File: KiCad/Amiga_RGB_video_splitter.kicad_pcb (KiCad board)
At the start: 4 copper layers, 57.5 x 60 mm, 26 parts, among them J1 DB23_Female-Connector, J2 DB15_Female_HighDensity_Mount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, J3 KMDGX-9S-BS-1, J4 PJ-320A, J5 MSS22D18 3Pin Slide Toggle Sw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, J6 MSS22D18 3Pin Slide Toggle Sw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, U1 THS7374IPWR, U2 74HCT2G17, U3 74HCT2G14, U4 74LVC1GX04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

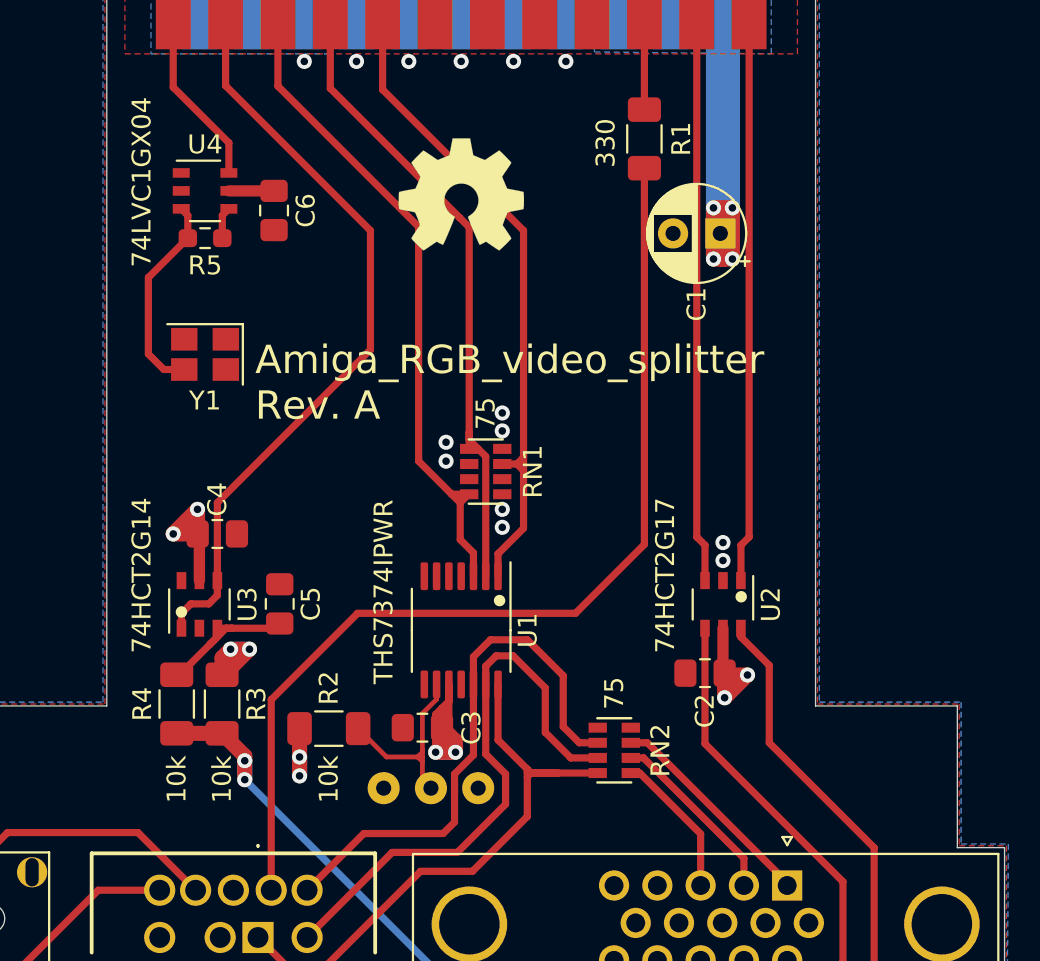
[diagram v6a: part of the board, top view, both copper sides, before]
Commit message: Add capacitor C7 and C8, and some silkscreen fixes
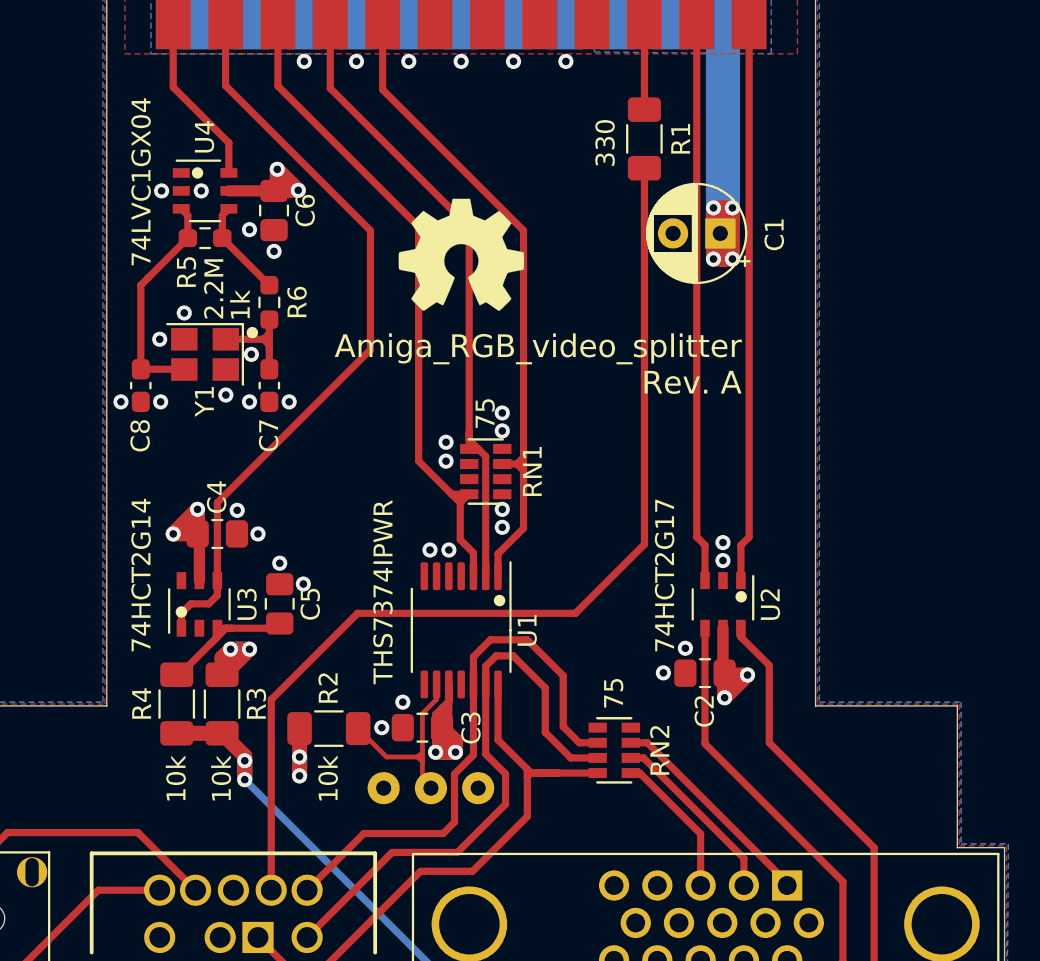
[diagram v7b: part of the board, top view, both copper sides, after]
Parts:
- added C7: 32pF, Capacitor_SMD:C_0603_1608Metric_Pad1.08x0.95mm_HandSolder, F.Cu at (137.6, 107.0)
- added C8: 32pF, Capacitor_SMD:C_0603_1608Metric_Pad1.08x0.95mm_HandSolder, F.Cu at (130.8, 107.0)
- added R6: 1k, Resistor_SMD:R_0603_1608Metric_Pad0.98x0.95mm_HandSolder, F.Cu at (137.6, 102.7)
- moved REF** 3.20 mm to (147.7, 100.2)
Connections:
- Y1 pad 1: Net-(R5-Pad2) -> Net-(C7-Pad1)
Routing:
- net Net-(C7-Pad1): track 0.00 -> 5.72 mm
- net VCC: track 102.0 -> 106.0 mm, vias 14 -> 16
- net Net-(R5-Pad2): track 1.69 -> 5.21 mm
- net Net-(C8-Pad1): track 10.9 -> 12.0 mm
- net GND: vias 14 -> 36
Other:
- board text added: "1k"
- board text added: "2.2M"

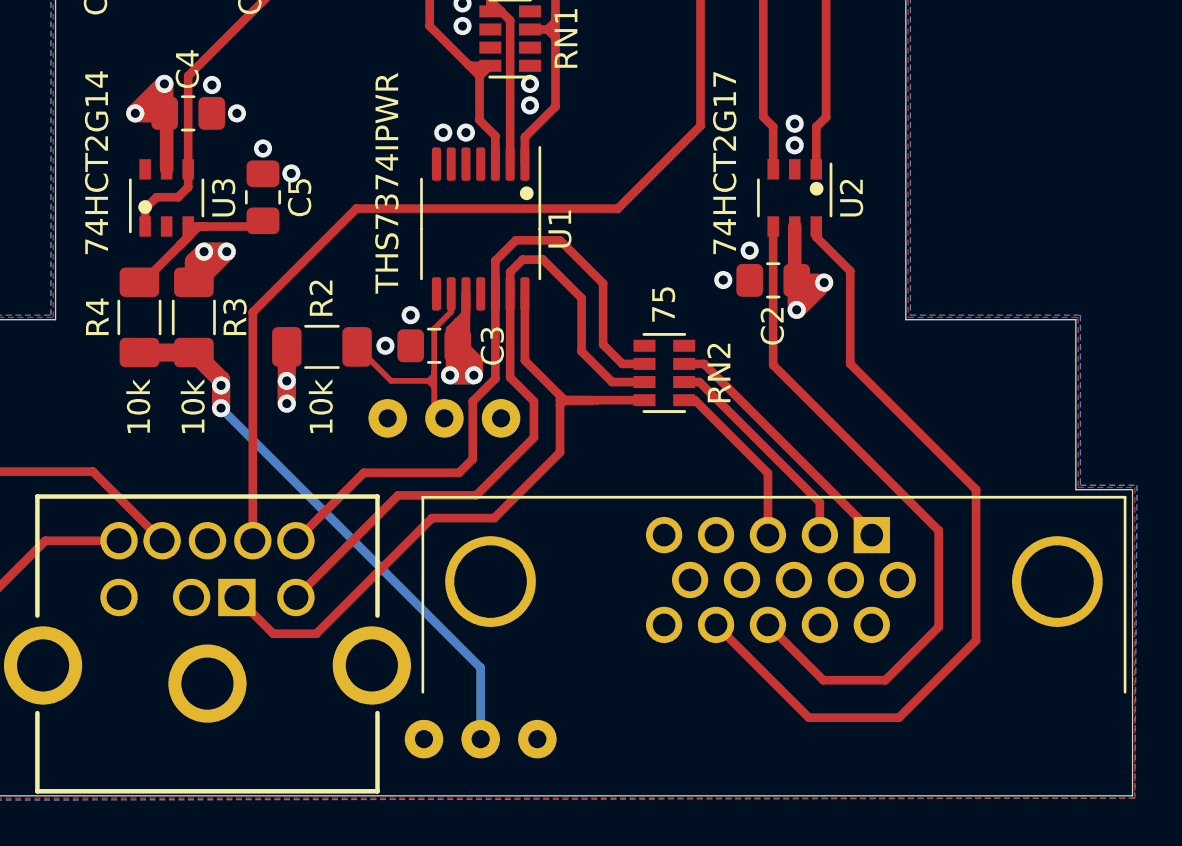
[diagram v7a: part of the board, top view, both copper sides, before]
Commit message: Add solder jumper JP1 to the design and route signals XCLKEN and OE to it
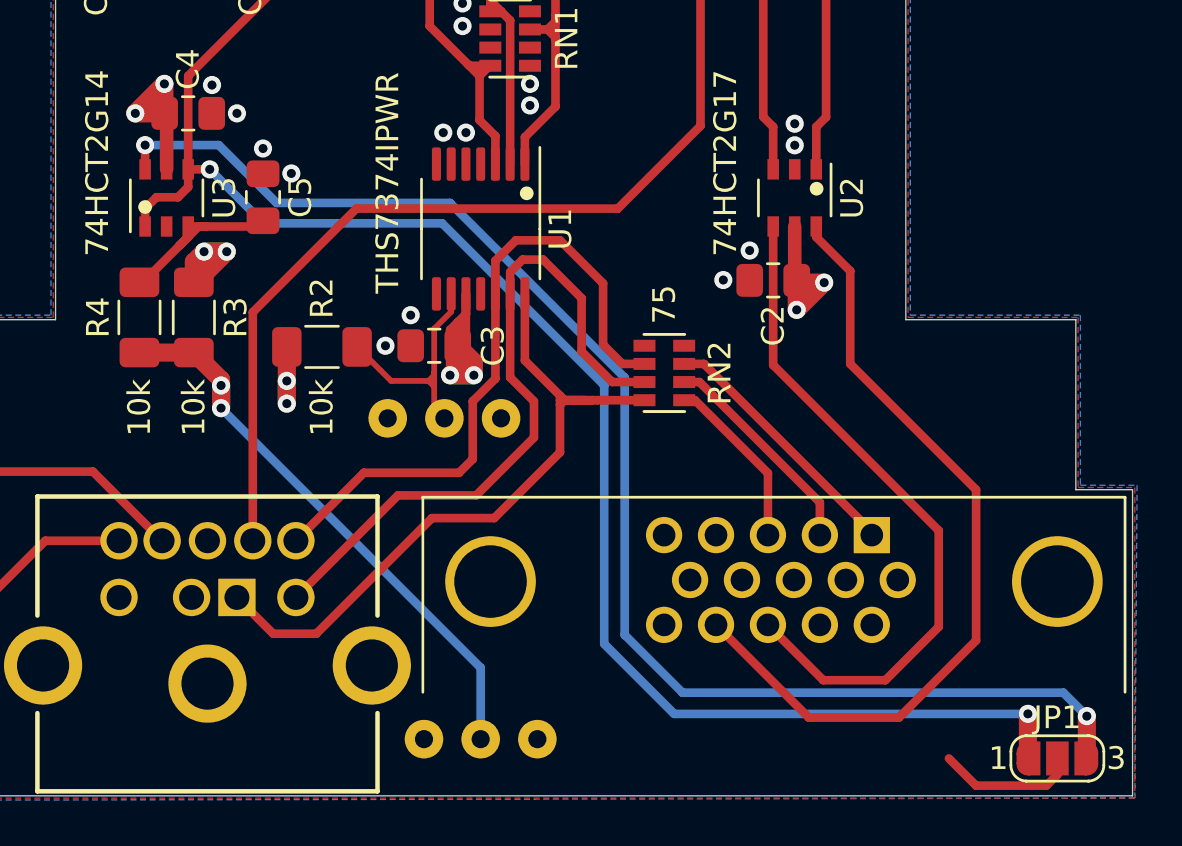
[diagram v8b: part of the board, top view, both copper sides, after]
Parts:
- added JP1: SolderJumper_3_Open, Jumper:SolderJumper-3_P1.3mm_Open_RoundedPad1.0x1.5mm_NumberLabels, F.Cu at (173.1, 143.3)
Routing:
- net OE: track 0.00 -> 61.6 mm, vias 0 -> 2
- net XCLKEN: track 40.5 -> 96.1 mm, vias 0 -> 2
- net Net-(JP1-Pad2): track 0.00 -> 6.20 mm
